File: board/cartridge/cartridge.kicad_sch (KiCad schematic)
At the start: 29 parts, among them J1 Foxconn_WQ21823-DES1-7F, J2 ZX-TYPEC-WCM1648, J3 Conn_ARM_JTAG_SWD_10, SW1 SW_Push, SW2 SW_SPDT, U1 AMS1117-3.3, U2 STM32G0B0RETx, U3 74LVC1G07, U4 NAU8814Y, Y1 Crystal

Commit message: Update schematic info block and add a README.
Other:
- title: TRS-80 CoCo2 Cart Emulator -> CoCo Chameleon - Cartridge Emulator

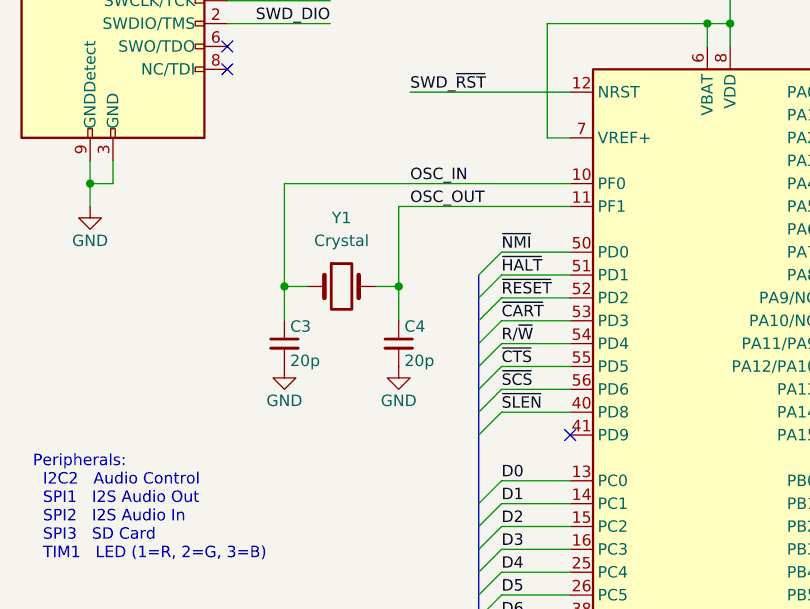
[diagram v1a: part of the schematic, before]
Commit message: Place and route MCU power and crystal.
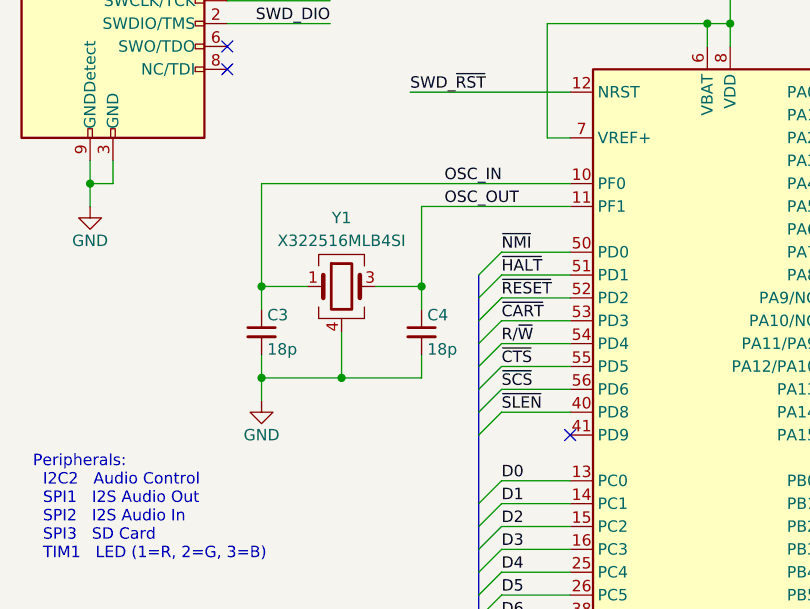
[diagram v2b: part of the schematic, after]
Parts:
- C3, C4: value 20p -> 18p
- P1: value ~ -> CardEdge
- Y1: value Crystal -> X322516MLB4SI; footprint (none) -> Crystal:Crystal_SMD_3225-4Pin_3.2x2.5mm; symbol Device:Crystal -> Device:Crystal_GND24; LCSC (none) -> C13738
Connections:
- net GND: now also Y1.2, Y1.4
- net OSC_OUT: now also Y1.3; no longer Y1.2
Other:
- moved on the sheet: C3, C4

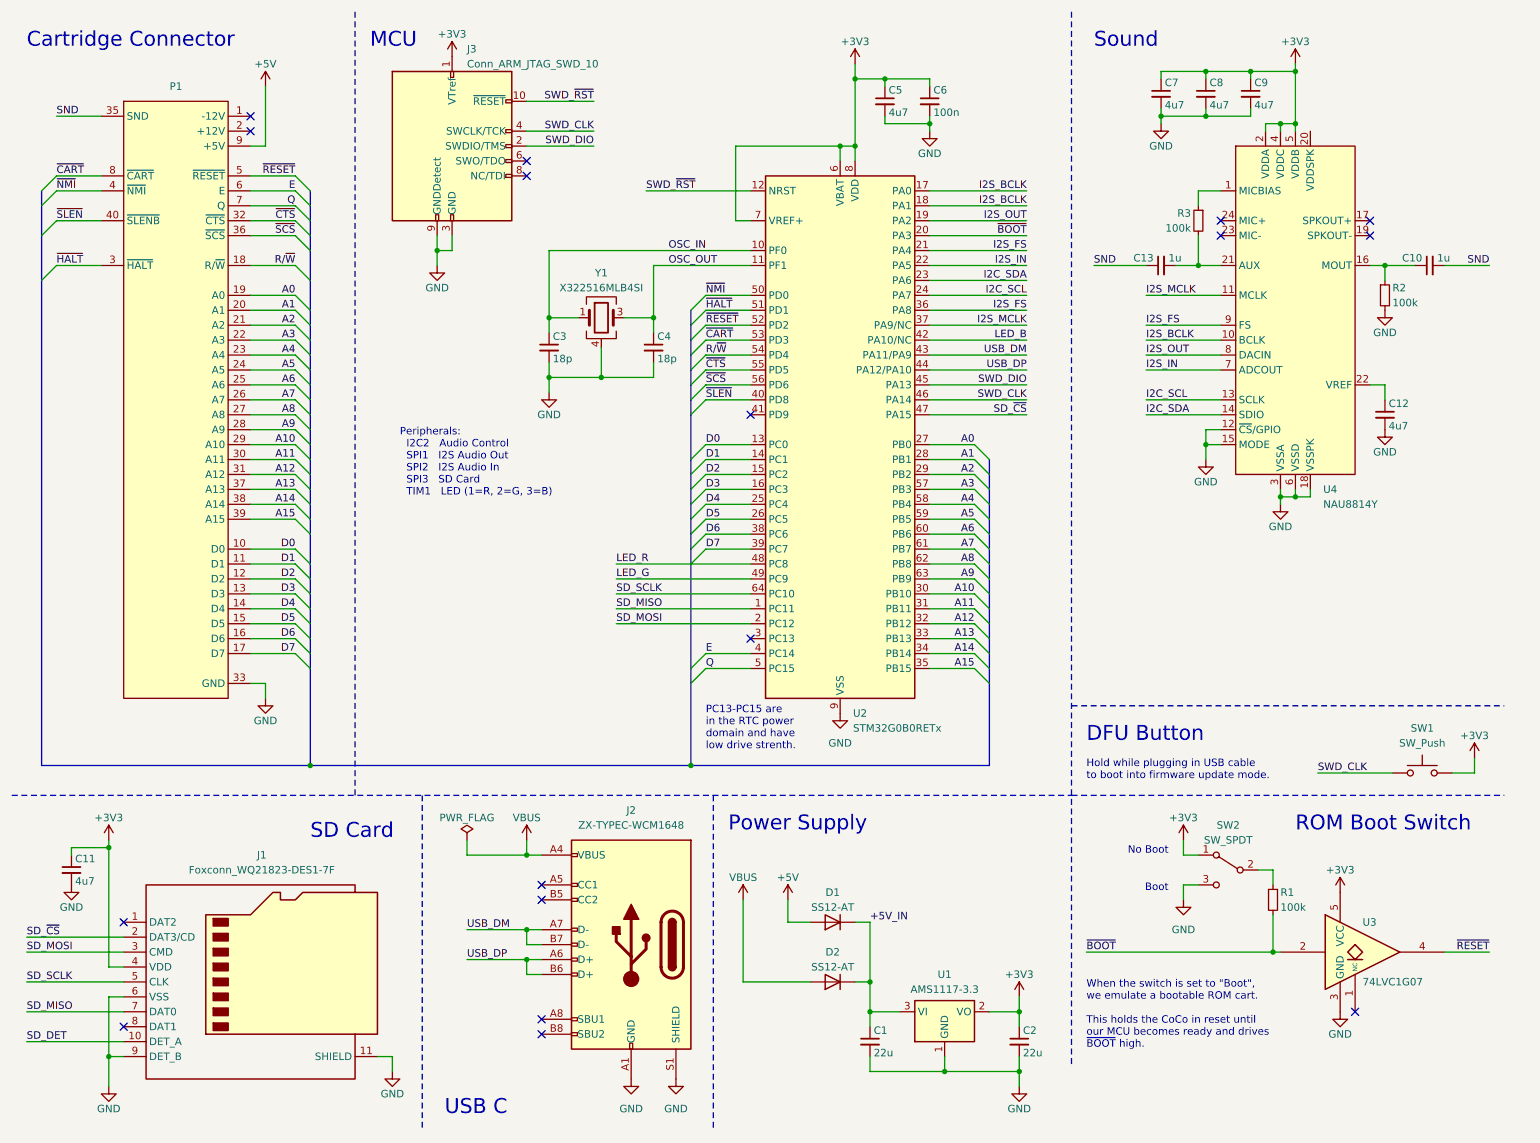
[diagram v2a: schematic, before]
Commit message: Choose parts for everything plus more routing.
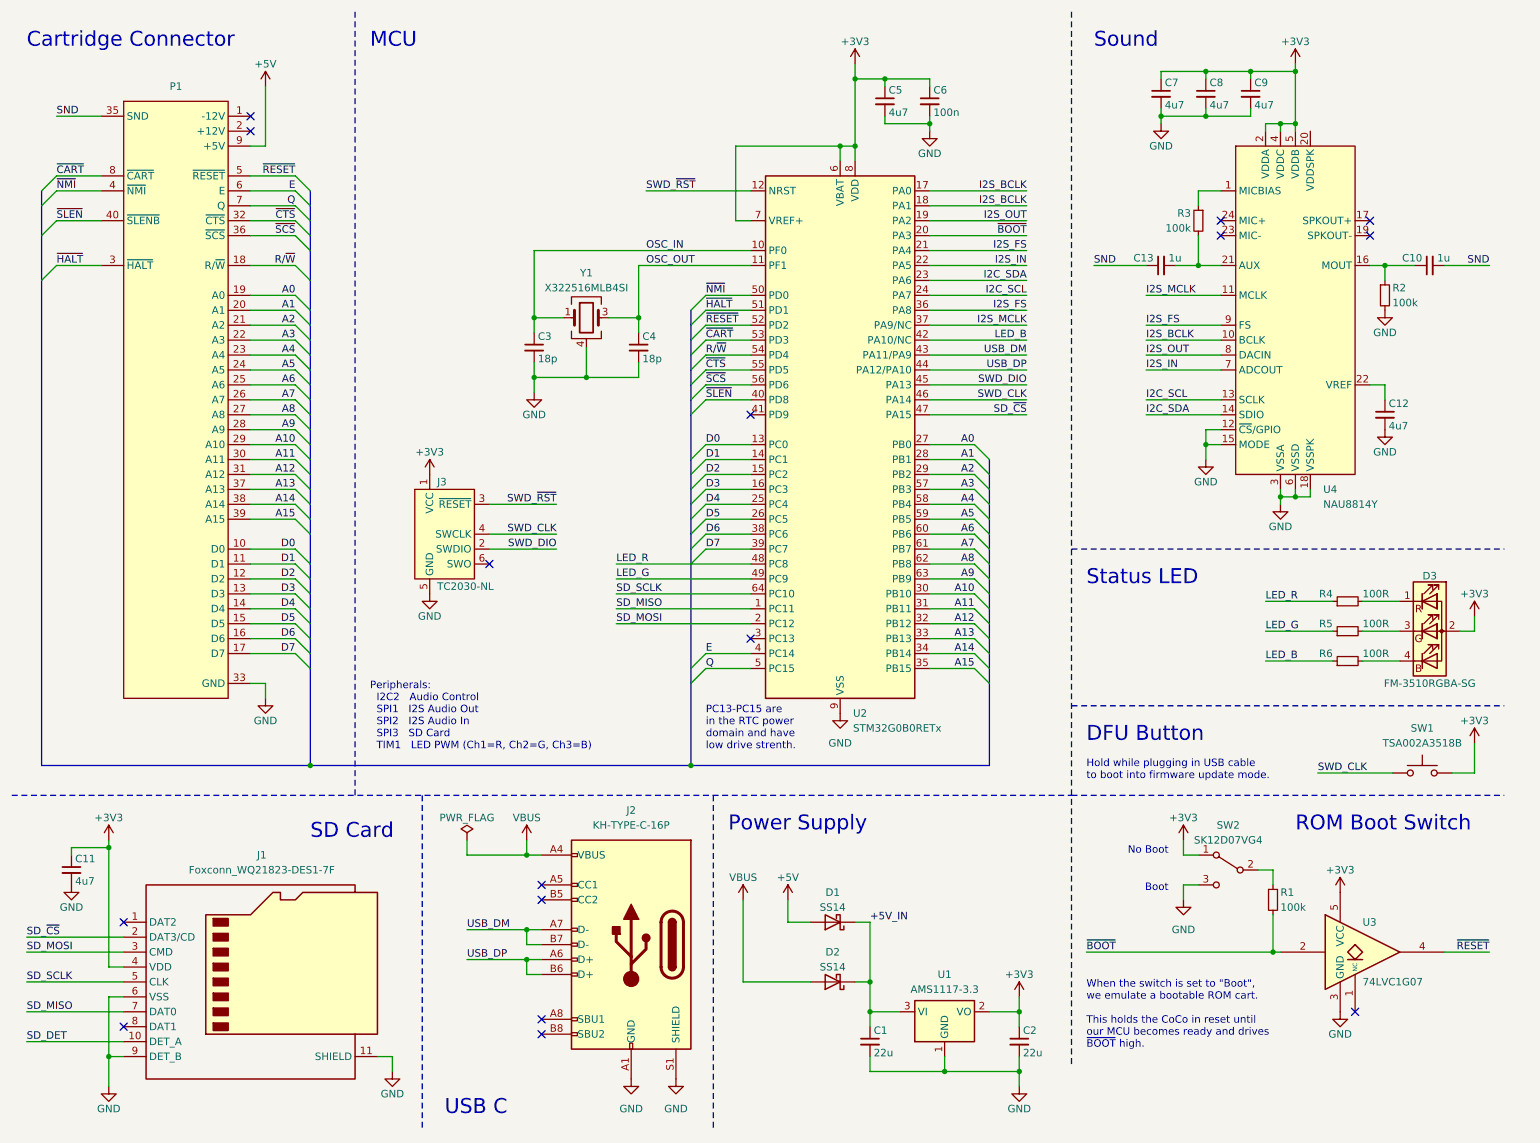
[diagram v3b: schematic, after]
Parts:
- removed D2: SS12-AT, Diode_SMD:D_SMA, symbol Device:D
- removed J3: Conn_ARM_JTAG_SWD_10, symbol Connector:Conn_ARM_JTAG_SWD_10
- added D2: SS14, Diode_SMD:D_SMA, symbol Device:D_Schottky
- added D3: FM-3510RGBA-SG, 0Project:FM-3510RGBA-SG, symbol Device:LED_RAGB
- added J3: TC2030-NL, Connector:Tag-Connect_TC2030-IDC-NL_2x03_P1.27mm_Vertical, symbol Connector:Conn_ARM_SWD_TagConnect_TC2030-NL
- added R4, R5, R6: 100R, Resistor_SMD:R_0603_1608Metric, symbol Device:R_Small
- D1: value SS12-AT -> SS14; symbol Device:D -> Device:D_Schottky; LCSC C2840970 -> C2480
- J2: value ZX-TYPEC-WCM1648 -> KH-TYPE-C-16P; footprint (none) -> 0Project:KH-TYPE-C-16P; LCSC C7419861 -> C709357
- SW1: value SW_Push -> TSA002A3518B; footprint (none) -> 0Project:TSA002A3518B; LCSC (none) -> C2846757
- SW2: value SW_SPDT -> SK12D07VG4; footprint (none) -> 0Project:SK12D07VG4; LCSC (none) -> C393937
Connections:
- net +3V3: now also D3.2 (A), J3.1 (VCC)
- net +5V_IN: now also D2.1 (K)
- net GND: now also J3.5 (GND)
- net LED_B: now also R6.1
- net LED_G: now also R5.1
- net LED_R: now also R4.1
- net SWD_CLK: now also J3.4 (SWCLK)
- net SWD_DIO: now also J3.2 (SWDIO)
- net SWD_~{RST}: now also J3.3 (~{RESET})
- net VBUS: now also D2.2 (A)
- new net: D3.4 (BK), R6.2
- new net: D3.1 (RK), R4.2
- new net: D3.3 (GK), R5.2
- no-connect marks 17 -> 16
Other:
- note added: "Peripherals: I2C2 Audio Control SPI1 I2S Audio Out SPI2 I2S Audio In SPI3 SD Card TIM1 LED PWM (Ch1=R, Ch2=G, Ch3=B)"
- note added: "Status LED"
- note removed: "Peripherals: I2C2 Audio Control SPI1 I2S Audio Out SPI2 I2S Audio In SPI3 SD Card TIM1 LED (1=R, 2=G, 3=B)"
- moved on the sheet: C3, C4, Y1

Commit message: Adjust layout based on an actual Tandy cartridge.
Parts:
- J1: value Foxconn_WQ21823-DES1-7F -> WQ21823-DES1-7F
- U4: footprint Package_DFN_QFN:VQFN-24-1EP_4x4mm_P0.5mm_EP2.5x2.5mm_ThermalVias -> Package_DFN_QFN:VQFN-24-1EP_4x4mm_P0.5mm_EP2.5x2.5mm
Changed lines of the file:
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@@
       (effects (font (size 1.27 1.27)))
     )
-    (property "Value" "Foxconn_WQ21823-DES1-7F" (at 55.245 158.75 0)
+    (property "Value" "WQ21823-DES1-7F" (at 55.245 158.75 0)
       (effects (font (size 1.27 1.27)))
     )
@@
       (effects (font (size 1.27 1.27)) (justify left))
     )
-    (property "Footprint" "Package_DFN_QFN:VQFN-24-1EP_4x4mm_P0.5mm_EP2.5x2.5mm_ThermalVias" (at 231.14 20.32 0)
-      (effects (font (size 1.27 1.27)) hide)
-    )
+    (property "Footprint" "Package_DFN_QFN:VQFN-24-1EP_4x4mm_P0.5mm_EP2.5x2.5mm" (at 231.14 20.32 0)
+      (effects (font (size 1.27 1.27)) hide)
+    )

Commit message: Another attempt at routing.
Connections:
- net +3V3: now also U4.20 (VDDSPK)
- net USB_DM renamed USB_DN
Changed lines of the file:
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@@
   (junction (at 228.6 31.75) (diameter 0) (color 0 0 0 0)
   )
+  (junction (at 233.68 31.75) (diameter 0) (color 0 0 0 0)
+  )
   (junction (at 158.75 182.88) (diameter 0) (color 0 0 0 0)
   )
@@
   (junction (at 119.38 64.77) (diameter 0) (color 0 0 0 0)
   )
-  (junction (at 231.14 22.86) (diameter 0) (color 0 0 0 0)
+  (junction (at 233.68 22.86) (diameter 0) (color 0 0 0 0)
   )
   (no_connect (at 31.75 185.42))
@@
     (stroke (width 0) (type default))
   )
+  (wire (pts (xy 233.68 31.75) (xy 231.14 31.75))
+    (stroke (width 0) (type default))
+  )
   (wire (pts (xy 168.91 111.76) (xy 176.53 111.76))
     (stroke (width 0) (type default))
@@
     (stroke (width 0) (type default))
   )
-  (wire (pts (xy 223.52 22.86) (xy 231.14 22.86))
+  (wire (pts (xy 223.52 22.86) (xy 233.68 22.86))
     (stroke (width 0) (type default))
   )
@@
     (stroke (width 0) (type default))
   )
+  (wire (pts (xy 233.68 31.75) (xy 233.68 33.02))
+    (stroke (width 0) (type default))
+  )
   (wire (pts (xy 130.81 86.36) (xy 138.43 86.36))
     (stroke (width 0) (type default))
@@
     (stroke (width 0) (type default))
   )
-  (wire (pts (xy 231.14 21.59) (xy 231.14 22.86))
+  (wire (pts (xy 233.68 21.59) (xy 233.68 22.86))
     (stroke (width 0) (type default))
   )
@@
     (stroke (width 0) (type default))
   )
-  (wire (pts (xy 231.14 31.75) (xy 231.14 22.86))
+  (wire (pts (xy 233.68 31.75) (xy 233.68 22.86))
     (stroke (width 0) (type default))
   )
@@
     (effects (font (size 1.27 1.27)) (justify right bottom))
   )
-  (label "USB_DM" (at 185.42 71.12 180) (fields_autoplaced)
+  (label "USB_DN" (at 185.42 71.12 180) (fields_autoplaced)
     (effects (font (size 1.27 1.27)) (justify right bottom))
   )
@@
     (effects (font (size 1.27 1.27)) (justify left bottom))
   )
-  (label "USB_DM" (at 90.17 168.91 0) (fields_autoplaced)
+  (label "USB_DN" (at 90.17 168.91 0) (fields_autoplaced)
     (effects (font (size 1.27 1.27)) (justify left bottom))
   )
@@
     )
   )
-  (symbol (lib_id "power:+3V3") (at 231.14 21.59 0) (unit 1)
-    (in_bom yes) (on_board yes) (dnp no)
-    (property "Reference" "#PWR025" (at 231.14 25.4 0)
-      (effects (font (size 1.27 1.27)) hide)
-    )
-    (property "Value" "+3V3" (at 231.14 17.78 0)
+  (symbol (lib_id "power:+3V3") (at 233.68 21.59 0) (unit 1)
+    (in_bom yes) (on_board yes) (dnp no)
+    (property "Reference" "#PWR025" (at 233.68 25.4 0)
+      (effects (font (size 1.27 1.27)) hide)
+    )
+    (property "Value" "+3V3" (at 233.68 17.78 0)
       (effects (font (size 1.27 1.27)))
     )
-    (property "Footprint" "" (at 231.14 21.59 0)
-      (effects (font (size 1.27 1.27)) hide)
-    )
-    (property "Datasheet" "" (at 231.14 21.59 0)
-      (effects (font (size 1.27 1.27)) hide)
-    )
+    (property "Footprint" "" (at 233.68 21.59 0)
+      (effects (font (size 1.27 1.27)) hide)
+    )
+    (property "Datasheet" "" (at 233.68 21.59 0)
+      (effects (font (size 1.27 1.27)) hide)
+    )

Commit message: Move CoCo footprints up to project.
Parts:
- P1: value CardEdge -> Card Edge; footprint 0Local:CoCo_Cart -> 0Project:CoCo_Cart; symbol 0Local:CoCo_Cart -> 0Project:CoCo_Cart
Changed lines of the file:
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@@
     )
   )
-  (symbol (lib_id "0Local:CoCo_Cart") (at 40.64 66.04 0) (unit 1)
+  (symbol (lib_id "0Project:CoCo_Cart") (at 40.64 66.04 0) (unit 1)
     (in_bom no) (on_board yes) (dnp no) (fields_autoplaced)
     (property "Reference" "P1" (at 40.64 25.4 0)
       (effects (font (size 1.27 1.27)))
     )
-    (property "Value" "CardEdge" (at 45.72 40.64 0)
+    (property "Value" "Card Edge" (at 45.72 40.64 0)
       (effects (font (size 1.27 1.27)) hide)
     )
-    (property "Footprint" "0Local:CoCo_Cart" (at 45.72 40.64 0)
+    (property "Footprint" "0Project:CoCo_Cart" (at 45.72 40.64 0)
       (effects (font (size 1.27 1.27)) hide)
     )

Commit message: Update boot switches to support MultiPak.
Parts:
- removed D3: FM-3510RGBA-SG, 0Project:FM-3510RGBA-SG, symbol Device:LED_RAGB
- removed R1: 100k, Resistor_SMD:R_0603_1608Metric, symbol Device:R_Small
- removed SW1: TSA002A3518B, 0Project:TSA002A3518B, symbol Switch:SW_Push
- removed SW2: SK12D07VG4, 0Project:SK12D07VG4, symbol Switch:SW_SPDT
- removed U3: 74LVC1G07, Package_TO_SOT_SMD:SOT-353_SC-70-5, symbol 74xGxx:74LVC1G07
- added D3: KT-0603R, LED_SMD:LED_0603_1608Metric, symbol Device:LED
- added D4: 19-217/GHC-YR1S2/3T, LED_SMD:LED_0603_1608Metric, symbol Device:LED
- added D5: 19-217/BHC-ZL1M2RY/3T, LED_SMD:LED_0603_1608Metric, symbol Device:LED
- added SW1, SW2: K3-1410S, 0Project:K3-1410S, symbol 0Project:K3-1410S
- R4: value 100R -> 150R
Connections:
- net +3V3: now also SW1.3 (COM), SW1.4 (COM), SW2.3 (COM), SW2.4 (COM); no longer C9.1, U4.20 (VDDSPK)
- net +5V: now also C9.1, U4.20 (VDDSPK), D3.2 (A), D4.2 (A), D5.2 (A)
- net SWD_CLK: now also SW2.6 (4)
- net at R6.2: now also D5.1 (K)
- net at R4.2: now also D3.1 (K)
- net at R5.2: now also D4.1 (K)
- net PAK_1: now reaches U2.3 (PC13)
- net PAK_1: now also SW1.5 (3)
- net PAK_0: now reaches U2.41 (PD9)
- net PAK_0: now also SW1.2
- no-connect marks 16 -> 15
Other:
- note added: "BASIC"
- note added: "Boot Mode Switch"
- note added: "Menu"
- note added: "Pak"
- note added: "Pak 1"
- note added: "Pak 2"
- note added: "Pak 3"
- note added: "Pak 4"
- note added: "Pak Select Switch"
- note added: "USB"
- note removed: "Boot"
- note removed: "DFU Button"
- note removed: "Hold while plugging in USB cable to boot into firmware update mode."
- note removed: "No Boot"
- note removed: "ROM Boot Switch"
- note removed: "When the switch is set to "Boot", we emulate a bootable ROM cart. This holds the CoCo in reset until our MCU becomes ready and drives ~{BOOT} high."
- moved on the sheet: C7, C8, C9, R4, R5, R6

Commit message: Add missing LCSC numbers.
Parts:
- U2: LCSC (none) -> C3230954
- U4: LCSC (none) -> C2442471
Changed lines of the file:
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@@
+      (effects (font (size 1.27 1.27)) hide)
+    )
+    (property "LCSC" "C3230954" (at 153.67 86.36 0)
       (effects (font (size 1.27 1.27)) hide)
     )
@@
       (effects (font (size 1.27 1.27)) hide)
     )
+    (property "LCSC" "C2442471" (at 231.14 58.42 0)
+      (effects (font (size 1.27 1.27)) hide)
+    )
